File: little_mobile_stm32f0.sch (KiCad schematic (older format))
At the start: 1 part

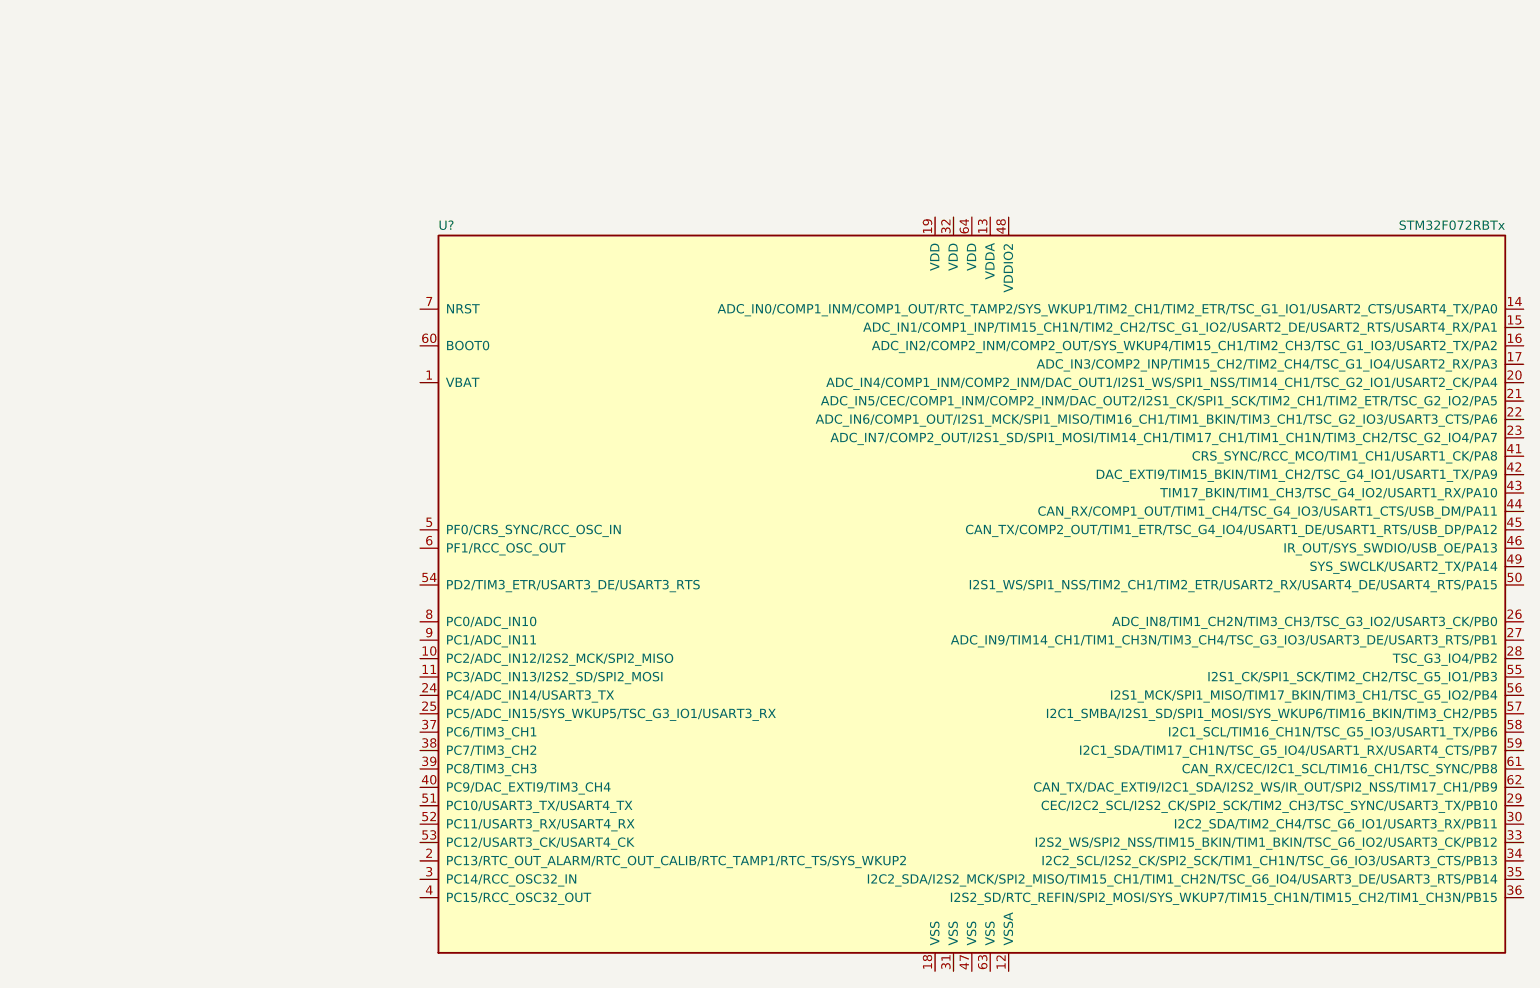
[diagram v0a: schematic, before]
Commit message: initial setup complete using TI Parts for power 3v3 Regulated output by Buck/Boost converter, efficiency 85% to 91% board will by only solderable in oven TODO: battery protection not calculated TODO: calculate ILIM etc. for battery charging TODO: check values for buck/boost converter, specify parts according to TI Webbench TODO: TiT
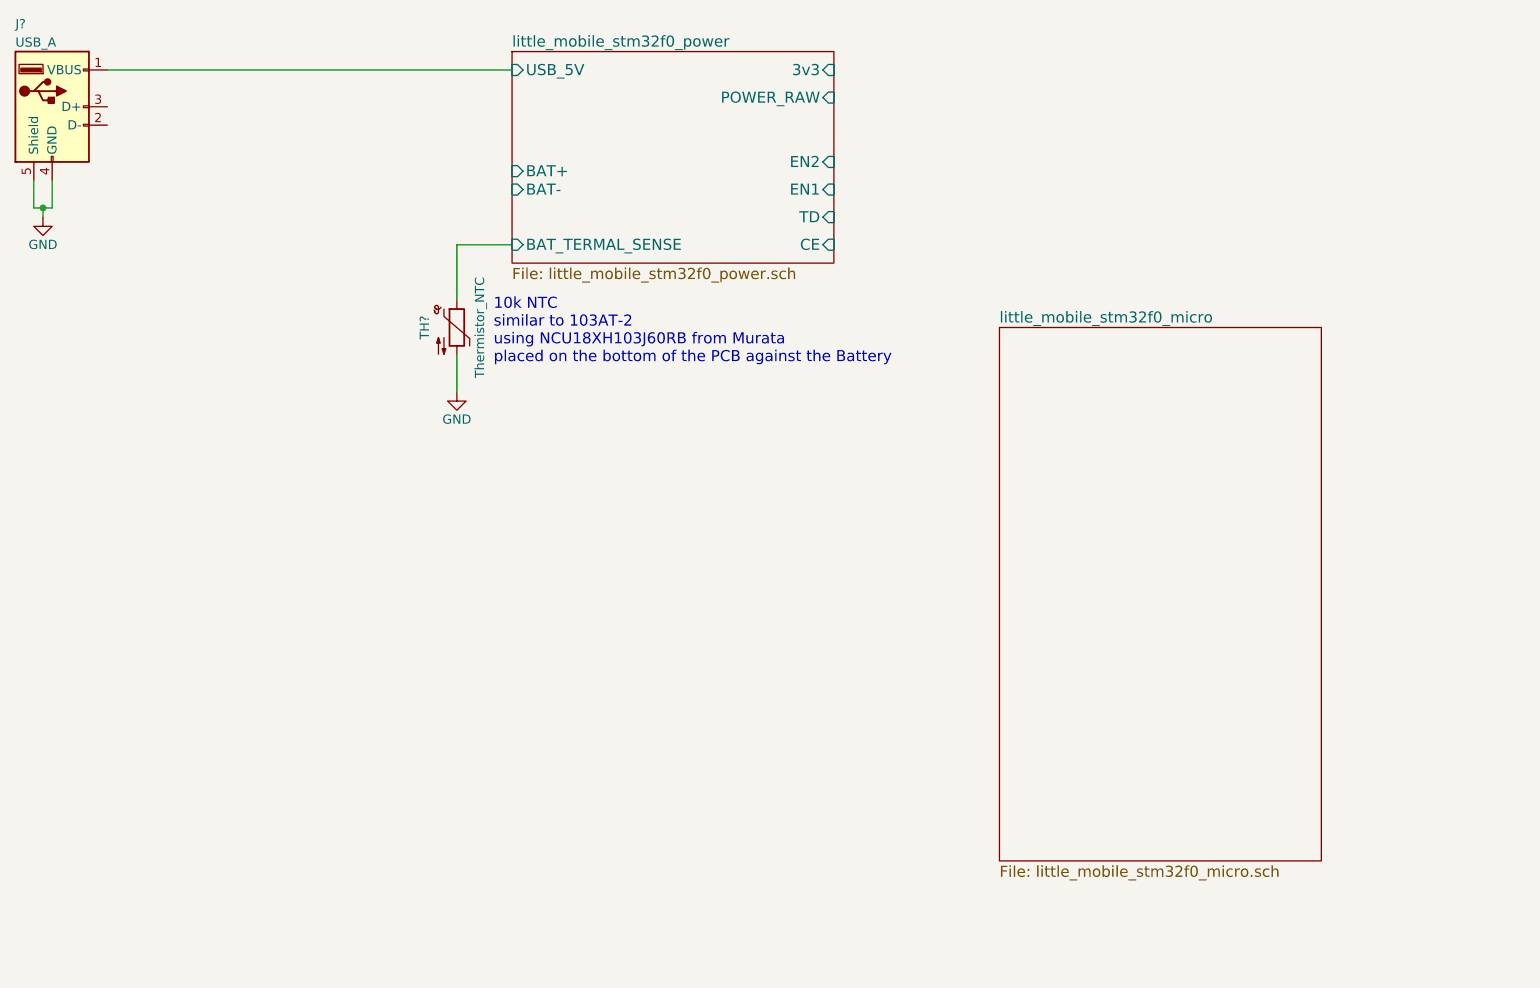
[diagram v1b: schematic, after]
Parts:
- removed U?: STM32F072RBTx, LQFP64, symbol STM32F072RBTx
- added J?: USB_A, symbol USB_A
- added TH?: Thermistor_NTC, symbol Thermistor_NTC
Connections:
- new net GND: J?.4 (GND), J?.5 (Shield), TH?.2
- new net little_mobile_stm32f0_power/BAT_TERMAL_SENSE: TH?.1
- new net little_mobile_stm32f0_power/USB_5V: J?.1 (VBUS)
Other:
- note added: "10k NTC\nsimilar to 103AT-2\nusing NCU18XH103J60RB from Murata\nplaced on the bottom of the PCB against the Battery"
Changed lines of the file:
@@
 LIBS:valves
 LIBS:MCU_ST_STM32
+LIBS:bq24073
+LIBS:bq29732
+LIBS:csd87313dms
+LIBS:tps63051rmw
+LIBS:switches
+LIBS:little_mobile_stm32f0-cache
 EELAYER 25 0
 EELAYER END
 $Descr A4 11693 8268
 encoding utf-8
-Sheet 1 1
+Sheet 1 3
 Title ""
 Date ""
@@
 Comment4 ""
 $EndDescr
+$Sheet
+S 3300 700  1750 1150
+U 5B77116C
+F0 "little_mobile_stm32f0_power" 60
+F1 "little_mobile_stm32f0_power.sch" 60
+F2 "USB_5V" I L 3300 800 60
+F3 "3v3" I R 5050 800 60
+F4 "POWER_RAW" I R 5050 950 60
+F5 "EN2" I R 5050 1300 60
+F6 "EN1" I R 5050 1450 60
+F7 "TD" I R 5050 1600 60
+F8 "CE" I R 5050 1750 60
+F9 "BAT-" I L 3300 1450 60
+F10 "BAT+" I L 3300 1350 60
+F11 "BAT_TERMAL_SENSE" I L 3300 1750 60
+$EndSheet
+$Sheet
+S 5950 2200 1750 2900
+U 5B7834FE
+F0 "little_mobile_stm32f0_micro" 60
+F1 "little_mobile_stm32f0_micro.sch" 60
+$EndSheet
 $Comp
-L STM32F072RBTx U?
-U 1 1 5A7F1001
-P 5800 3700
-F 0 "U?" H 2900 5725 50  0000 L BNN
-F 1 "STM32F072RBTx" H 8700 5725 50  0000 R BNN
-F 2 "LQFP64" H 8700 5675 50  0001 R TNN
-F 3 "" H 5800 3700 50  0001 C CNN
-	1    5800 3700
+L USB_A J?
+U 1 1 5B78483D
+P 800 1000
+F 0 "J?" H 600 1450 50  0000 L CNN
+F 1 "USB_A" H 600 1350 50  0000 L CNN
+F 2 "" H 950 950 50  0001 C CNN
+F 3 "" H 950 950 50  0001 C CNN
+	1    800  1000
 	1    0    0    -1
 $EndComp
+Wire Wire Line
+	1100 800  3300 800
+Wire Wire Line
+	700  1400 700  1550
+Wire Wire Line
+	700  1550 800  1550
+Wire Wire Line
+	800  1550 800  1400
+$Comp
+L GND #PWR?
+U 1 1 5B785365
+P 750 1600
+F 0 "#PWR?" H 750 1350 50  0001 C CNN
+F 1 "GND" H 750 1450 50  0000 C CNN
+F 2 "" H 750 1600 50  0001 C CNN
+F 3 "" H 750 1600 50  0001 C CNN
+	1    750  1600
+	1    0    0    -1
+$EndComp
+Wire Wire Line
+	750  1600 750  1550
+Connection ~ 750  1550
+$Comp
+L Thermistor_NTC TH?
+U 1 1 5B785F64
+P 3000 2200
+F 0 "TH?" V 2825 2200 50  0000 C CNN
+F 1 "Thermistor_NTC" V 3125 2200 50  0000 C CNN
+F 2 "" H 3000 2250 50  0001 C CNN
+F 3 "" H 3000 2250 50  0001 C CNN
+	1    3000 2200
+	1    0    0    -1
+$EndComp
+Text Notes 3200 2400 0    60   ~ 0
+10k NTC\nsimilar to 103AT-2\nusing NCU18XH103J60RB from Murata\nplaced on the bottom of the PCB against the Battery
+Wire Wire Line
+	3300 1750 3000 1750
+Wire Wire Line
+	3000 1750 3000 2050
+$Comp
+L GND #PWR?
+U 1 1 5B78645B
+P 3000 2550
+F 0 "#PWR?" H 3000 2300 50  0001 C CNN
+F 1 "GND" H 3000 2400 50  0000 C CNN
+F 2 "" H 3000 2550 50  0001 C CNN
+F 3 "" H 3000 2550 50  0001 C CNN
+	1    3000 2550
+	1    0    0    -1
+$EndComp
+Wire Wire Line
+	3000 2350 3000 2550
 $EndSCHEMATC
